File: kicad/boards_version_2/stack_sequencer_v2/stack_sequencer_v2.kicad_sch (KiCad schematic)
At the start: 10 parts

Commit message: Work on stack sequencer
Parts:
- added U11, U14: ~, Package_DIP:DIP-14_W7.62mm, symbol custom_symbol_lib:quad_and
- added U12, U13, U15: ~, Package_DIP:DIP-14_W7.62mm, symbol custom_symbol_lib:quad_OR
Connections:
- net at U7.12 (Q7): now also U11.9 (4B)
- net at U6.6 (D4), U7.13 (Q6): now also U1.15 (Pointer_++(0)_/_--_(1)), U11.13 (3A)
- net at U2.13 (Q6), U7.8 (D6): now also U11.1 (1A)
- net at U2.12 (Q7), U7.9 (D7): now also U5.5 (I2), U13.6 (1B)
- net at U6.15 (Q4): now also U11.12 (3B)
- net at U6.18 (Q1): now also U14.4 (2A)
- net at U6.19 (Q0): now also U13.13 (3B), U14.2 (1B)
- net at U6.2 (D0), U8.11 (3Q): now also U13.12 (3A), U14.1 (1A)
- net at U1.10 (TX_Offset_read), U6.3 (D1): now also U12.1 (0A), U15.1 (0A)
- net at U1.11 (TX_Get_offset), U6.5 (D3): now also U12.2 (0B)
- net at U1.3 (Enable), U4.1 (1A), U4.13 (3A)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: now also U11.4 (2A)
- net at U1.9 (TX_Pop), U2.8 (D6): now also U12.13 (3B), U12.5 (1A), U12.8 (2A)
- net at U2.9 (D7), U8.3 (1Q): now also U12.9 (2B)
- net at U5.6 (O2): now also U11.10 (4A)
- net at U1.12 (TX_Ready): now also U12.4 (Q1)
- net at U1.16 (Post-adder_latch_CLK): now also U13.4 (Q1)
- net at U1.17 (Memory_output_enable): now also U11.6 (2Q)
- net at U1.18 (Memory_write_enable): now also U13.10 (Q2)
- net at U1.19 (ToS_(0)_/_Offset_(1)_select): now also U15.4 (Q1)
- net at U1.22 (Pre-adder_latch_CLK): now also U12.10 (Q2)
- net at U1.5 (RX_Extend_(from_controller)): now also U11.2 (1B), U14.12 (3B), U14.5 (2B)
- new net: U12.11 (Q3), U13.1 (0A)
- new net: U13.11 (Q3), U15.5 (1A)
- new net: U13.2 (0B), U15.3 (Q0), U15.6 (1B)
- new net: U11.5 (2B), U13.3 (Q0)
- new net: U11.11 (3Q), U13.5 (1A)
- new net: U11.8 (4Q), U13.8 (2A)
- new net: U13.9 (2B), U14.3 (1Q)
- new net: U14.6 (2Q), U15.2 (0B)
- new net: U11.3 (1Q), U12.12 (3A)
- new net: U12.3 (Q0), U12.6 (1B)
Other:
- note added: "!falling 7"
- note added: "G12"
- note added: "G13"
- note added: "G14"
- note added: "G15"
- note added: "G16"
- note added: "G17"
- note added: "G18"
- note added: "G19"
- note added: "G20"
- note added: "G21"
- note added: "G22"
- note added: "G23"
- note added: "G24"
- note added: "G25"
- note added: "G29"
- note added: "G30"
- note added: "G31"
- note added: "G32"
- note added: "G33"

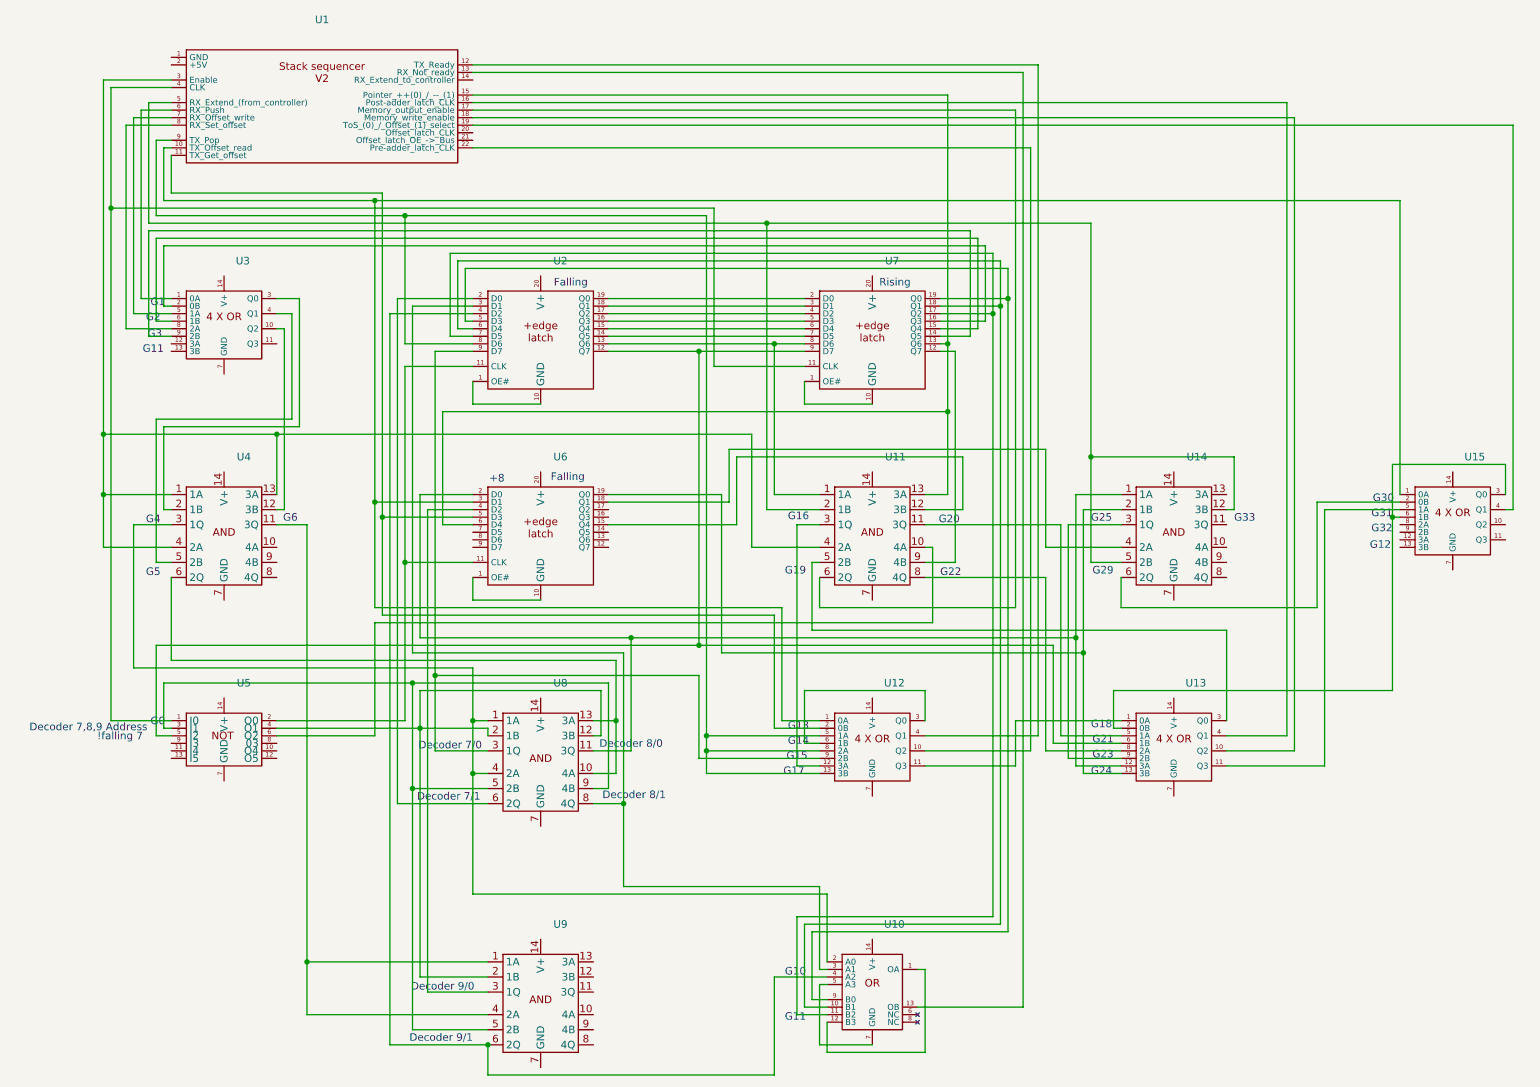
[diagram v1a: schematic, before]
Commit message: Stack circuit done not yet verified
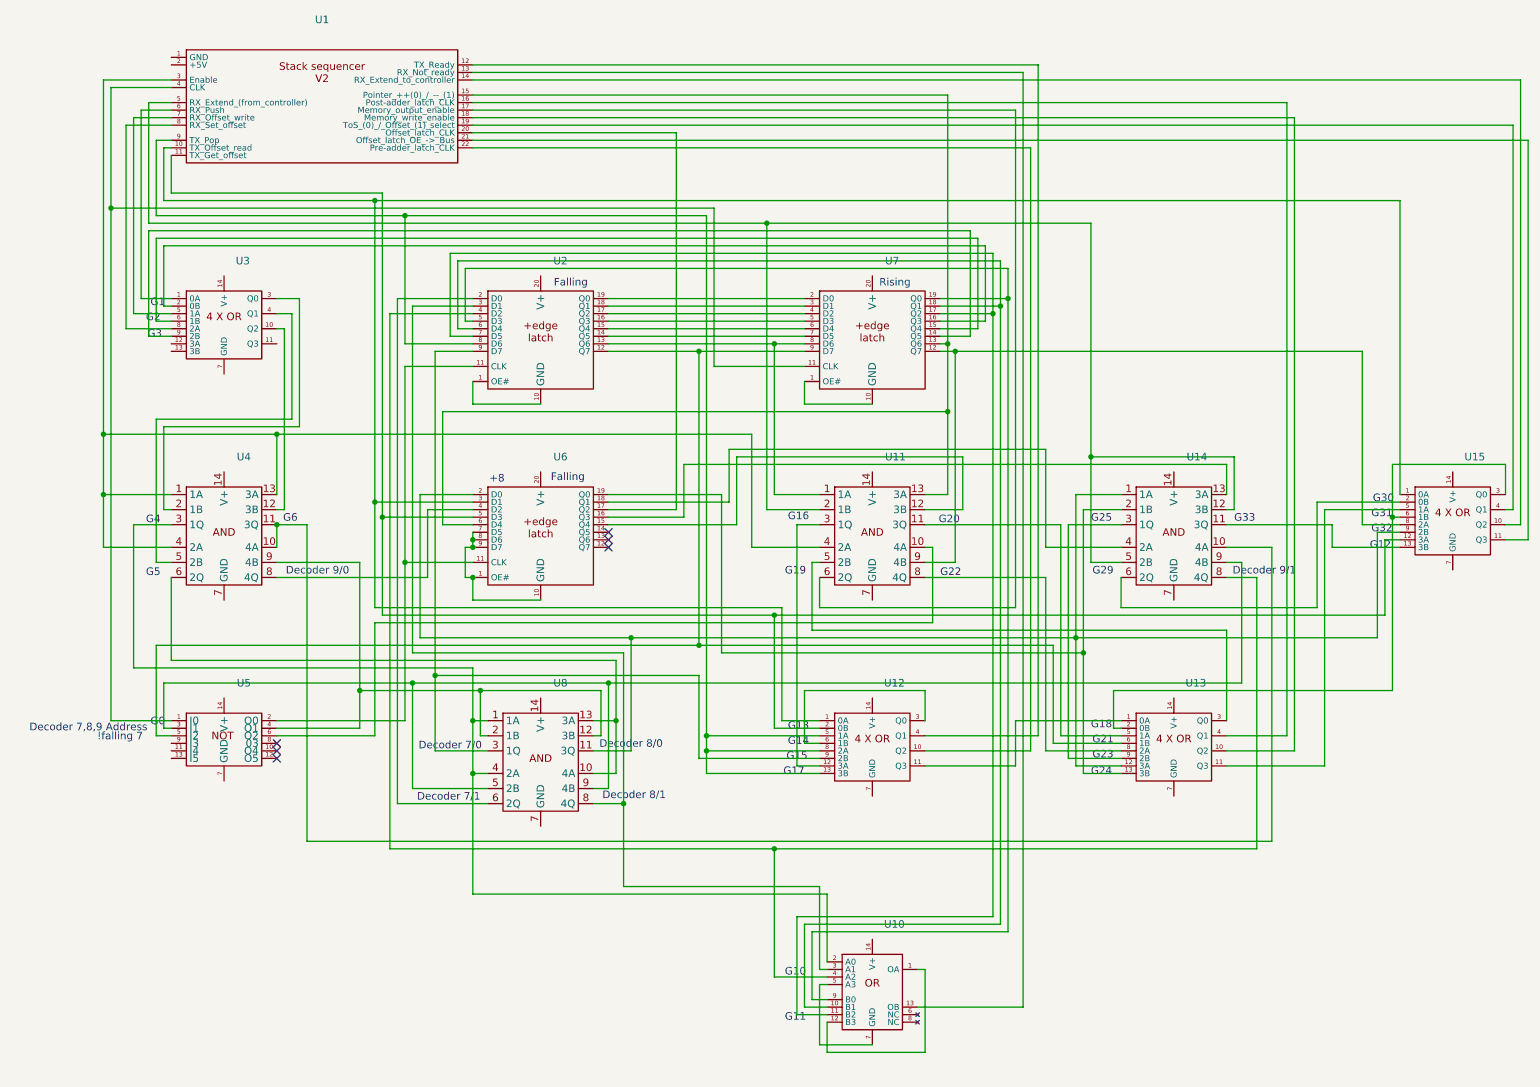
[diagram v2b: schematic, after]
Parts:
- removed U9: ~, Package_DIP:DIP-14_W7.62mm, symbol custom_symbol_lib:quad_and
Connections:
- net at U11.9 (4B), U7.12 (Q7): now also U15.8 (2A)
- net at U13.12 (3A), U14.1 (1A), U6.2 (D0)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: now also U15.9 (2B)
- net at U4.11 (3Q): now also U14.10 (4A), U4.10 (4A)
- net at U5.4 (O1), U8.12 (3B), U8.2 (1B): now also U4.9 (4B)
- net at U6.4 (D2): now also U4.8 (4Q)
- net at U5.3 (I1), U8.5 (2B), U8.9 (4B): now also U14.9 (4B)
- net at U10.4 (A2), U2.4 (D2): now also U14.8 (4Q)
- net at U14.11 (3Q): now also U15.13 (3B)
- net at U14.13 (3A): now also U6.16 (Q3)
- net at U6.1 (OE#), U6.10 (GND): now also U6.7 (D5), U6.8 (D6), U6.9 (D7)
- net at U6.17 (Q2): now also U1.20 (Offset_latch_CLK)
- net at U1.11 (TX_Get_offset), U12.2 (0B), U6.5 (D3): now also U15.12 (3A)
- net at U15.10 (Q2): now also U1.14 (RX_Extend_to_controller)
- net at U15.11 (Q3): now also U1.21 (Offset_latch_OE_->_Bus)
- no-connect marks 0 -> 6

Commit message: Stack sequencer verified
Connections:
- net at U3.12 (3A): now also U1.1 (GND), U10.5 (A3), U10.7 (GND), U11.7 (GND), U12.7 (GND), U13.7 (GND), U14.7 (GND), U15.7 (GND), U2.1 (OE#), U2.10 (GND), U3.13 (3B), U3.7 (GND), U4.7 (GND), U5.11 (I4), U5.13 (I5), U5.7 (GND), U5.9 (I3), U6.1 (OE#), U6.10 (GND), U6.7 (D5), U6.8 (D6), U6.9 (D7), U7.1 (OE#), U7.10 (GND), U8.7 (GND)
- net at U3.14 (V+): now also U1.2 (+5V), U10.14 (V+), U11.14 (V+), U12.14 (V+), U13.14 (V+), U14.14 (V+), U15.14 (V+), U2.20 (V+), U4.14 (V+), U5.14 (V+), U6.20 (V+), U7.20 (V+), U8.14 (V+)
- net at U14.9 (4B), U5.3 (I1), U8.5 (2B)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: now also U1.12 (TX_Ready), U12.4 (Q1)
- no-connect marks 6 -> 7
